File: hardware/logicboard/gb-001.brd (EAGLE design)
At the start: 100 x 76 mm, 8 parts

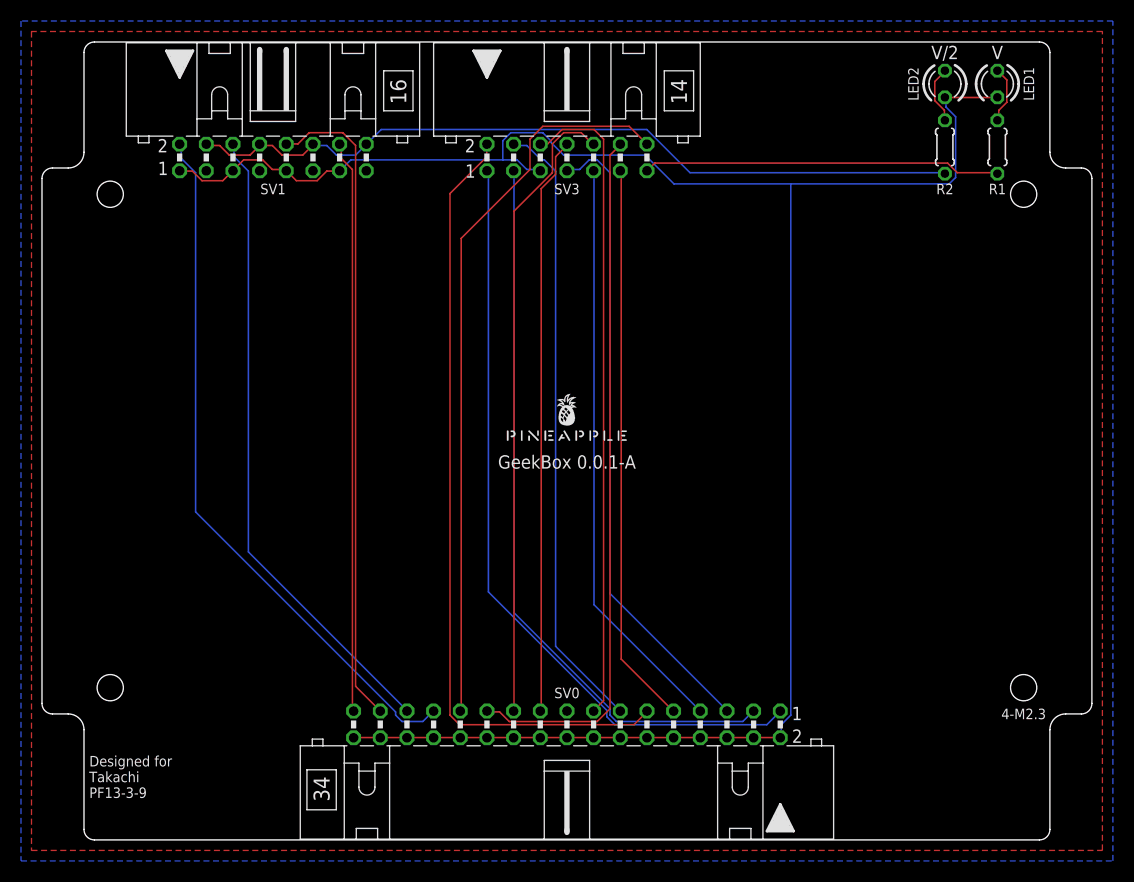
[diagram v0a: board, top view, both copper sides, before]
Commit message: Redesigned for PF10-2-7.
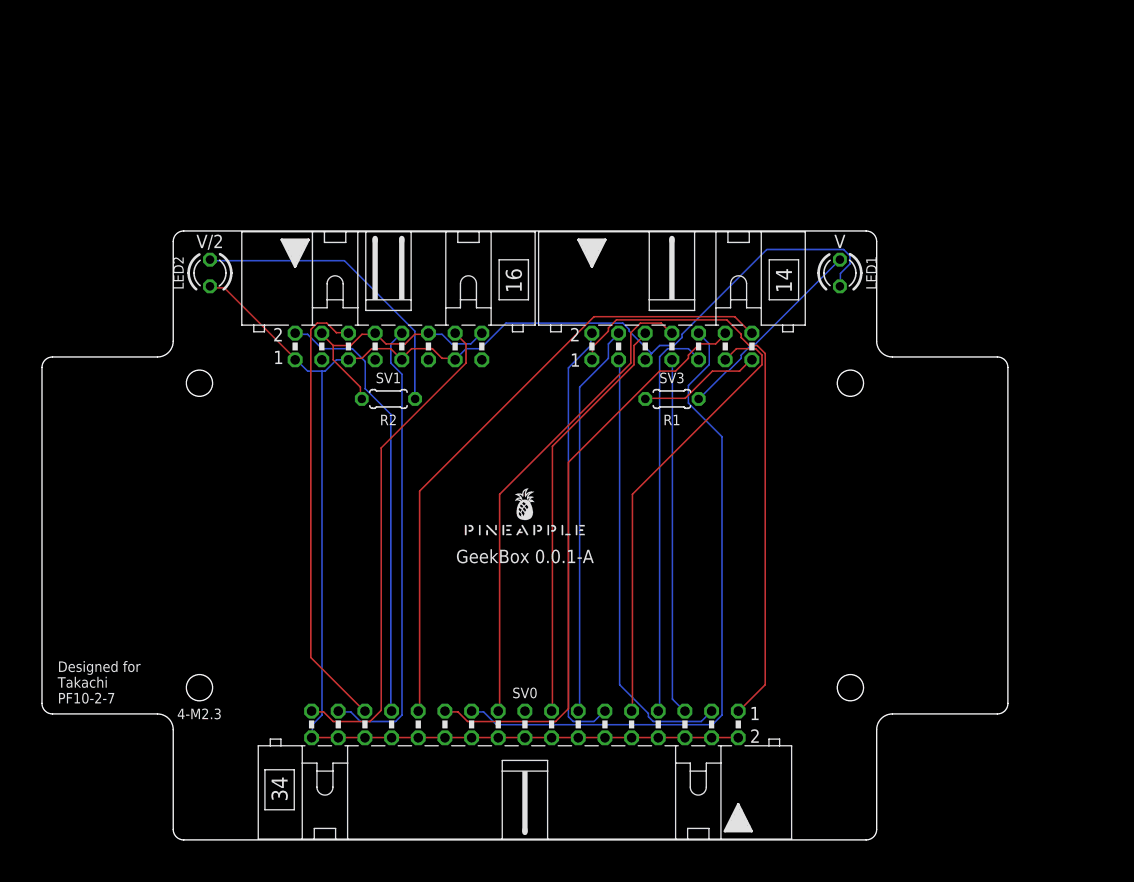
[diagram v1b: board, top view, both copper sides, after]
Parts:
- moved LED2 72.3 mm to (16.0, 54.0)
- moved R2 58.2 mm to (33.0, 42.0), turned to 0 degrees
- moved R1 39.2 mm to (60.0, 42.0), turned to 0 degrees
- moved LED1 23.4 mm to (76.0, 54.0)
- moved SV1 21.1 mm to (33.0, 47.0)
- moved SV3 20.6 mm to (60.0, 47.0)
- moved U$1 9.85 mm to (46.0, 29.0)
- moved SV0 4.00 mm to (46.0, 11.0)
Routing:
- net VCC/2: track 75.4 -> 24.3 mm
- net GND: track 192.4 -> 154.4 mm
- net T05: track 75.5 -> 41.5 mm
- net T01: track 70.0 -> 41.8 mm
- net T02: track 60.9 -> 34.0 mm
- net T12: track 67.2 -> 42.1 mm
- net VCC2LED: track 5.52 -> 28.9 mm
- net VCC: track 34.1 -> 11.7 mm
- net T07: track 61.9 -> 39.7 mm
- net T06: track 59.1 -> 37.6 mm
- net T00: track 74.2 -> 55.6 mm
- net T14: track 62.4 -> 44.0 mm
- net T13: track 60.9 -> 42.7 mm
- net T03: track 55.7 -> 38.3 mm
- net VCCLED: track 5.52 -> 19.1 mm
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- removed copper zone on layer 1, net GND
- removed copper zone on layer 16, net GND
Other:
- board size 100 x 76 mm -> 92 x 58 mm
- board text added: "Designed for Takachi PF10-2-7"
- board text removed: "Designed for Takachi PF13-3-9"
